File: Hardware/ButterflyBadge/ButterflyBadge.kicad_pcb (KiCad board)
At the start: 4 copper layers, 26.7 x 96.5 mm, 95 parts, among them J1 USB_C_Receptacle_USB2.0, J4 Conn_02x07_Odd_Even, M1 Motor_DC, P1 TC2030-CTX, Q1 ALS-PT19, Q2 Q_NMOS_GSD, SW1 SW_Push, SW3 SW_SPDT, U1 W25Q128JVS, U2 CN3058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

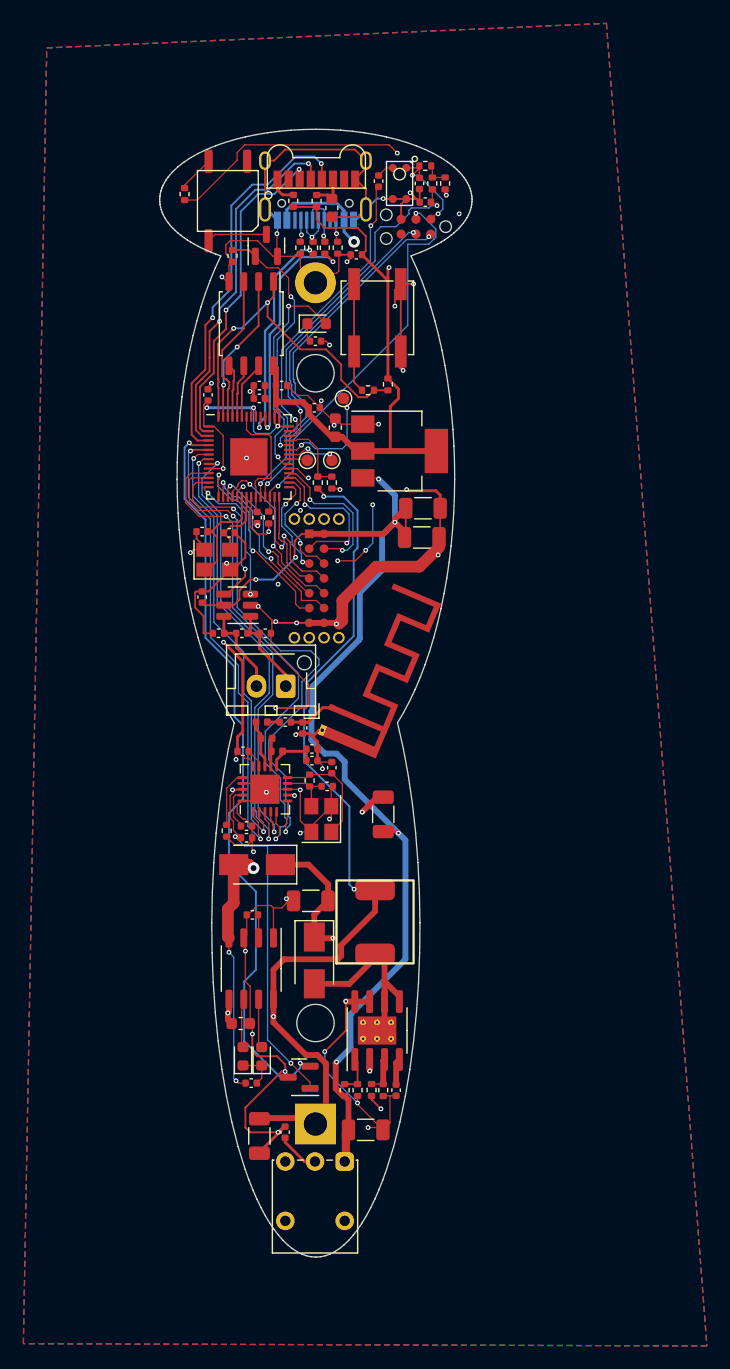
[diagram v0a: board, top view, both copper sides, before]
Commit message: Placed all the stbd wing leds
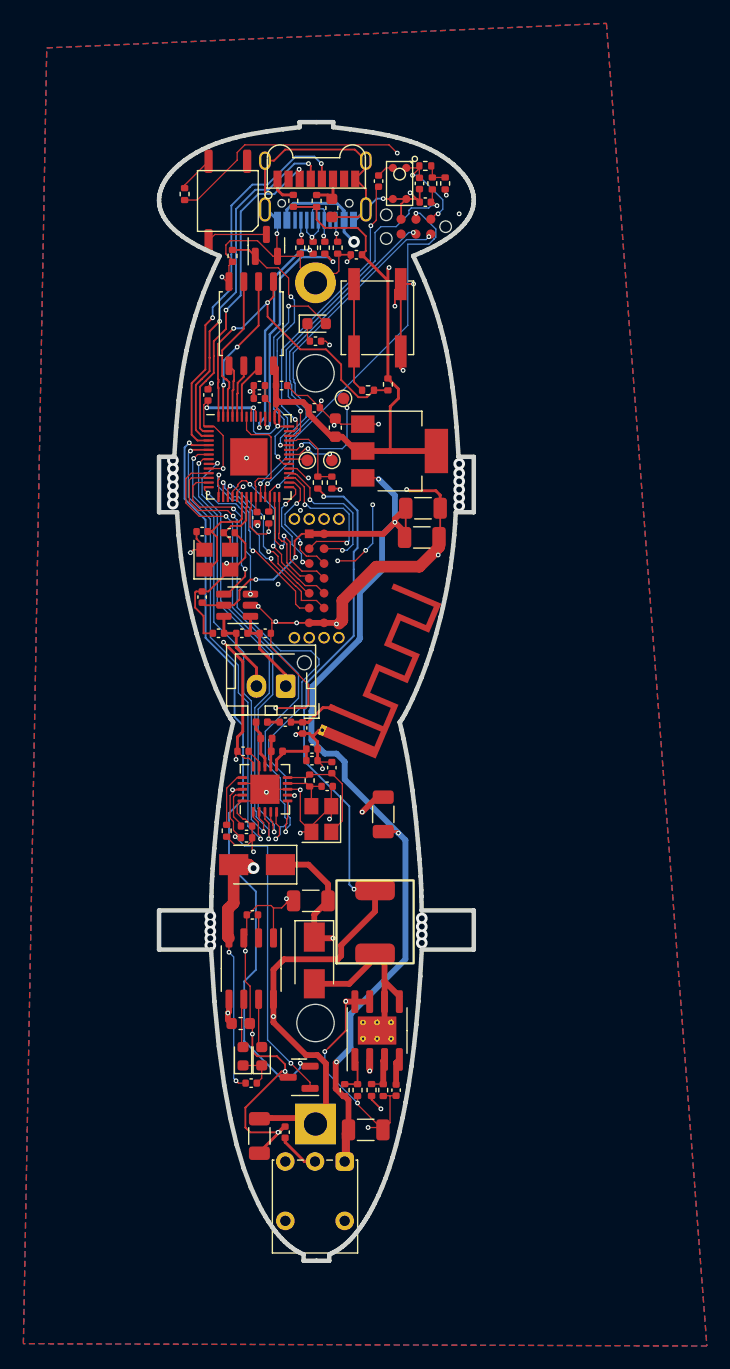
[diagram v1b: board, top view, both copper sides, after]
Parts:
- added G***: LOGO, ButterflyBadge:tiledBg, B.Cu at (194.1, 98.8)
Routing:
- net (no net): vias 0 -> 21
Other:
- board size 26.7 x 96.5 mm -> 26.9 x 97.4 mm
